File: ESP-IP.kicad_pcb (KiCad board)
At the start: 2 copper layers, 32 parts, among them J1 Serial and power, J2 Programming Pads, Q1 L78M05ABDT-TR, SW1 SW_Push, SW2 SW_Push, U1 ESP32-WROOM-32U, U3 TXS0102DCU, U4 AMS1117-3.3

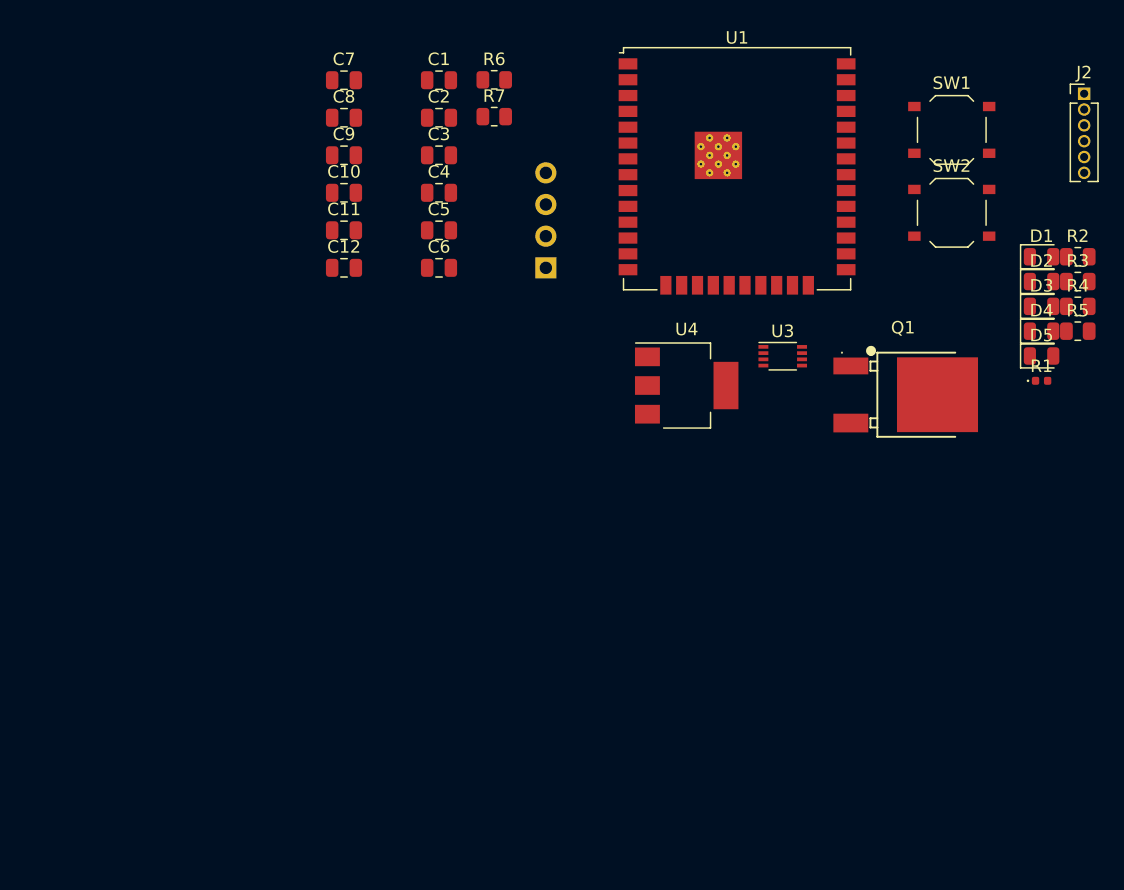
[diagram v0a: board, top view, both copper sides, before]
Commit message: my suggested board layout, includes schematic fixes, part number allocation and PCB, routing TBD
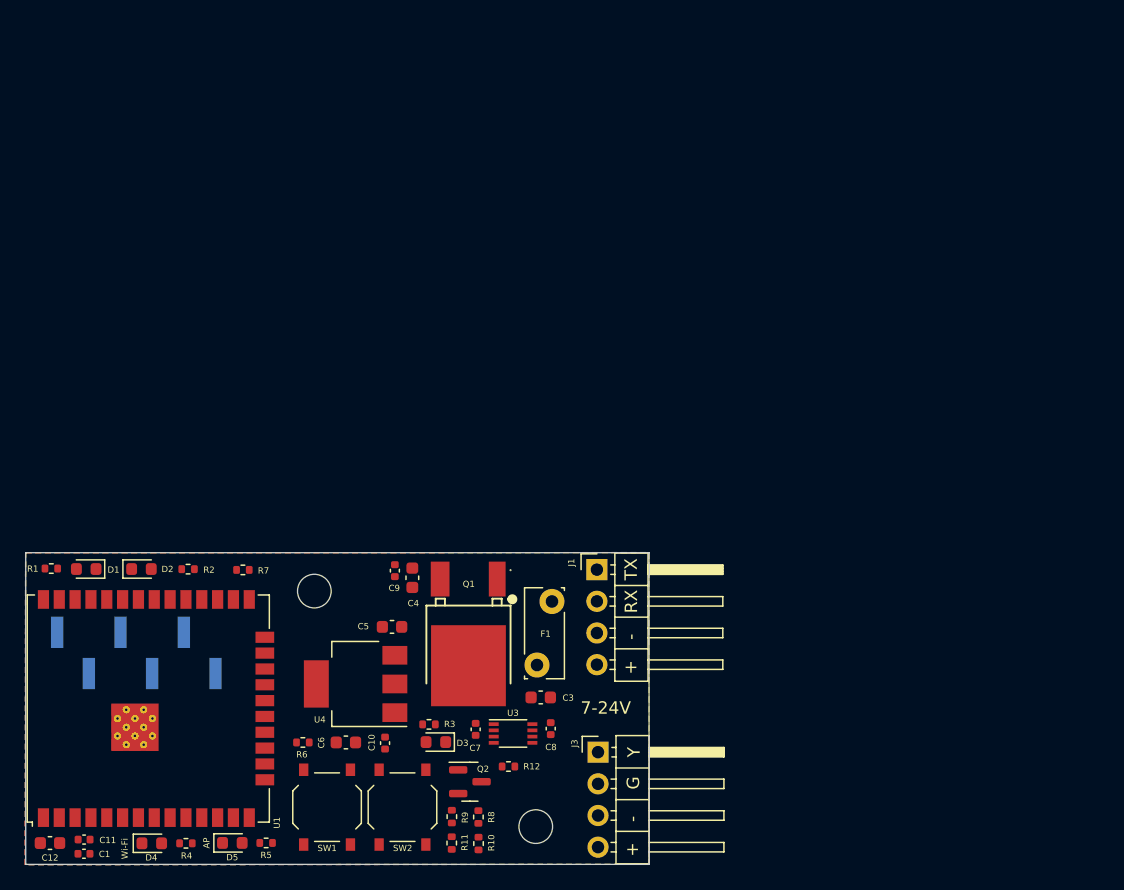
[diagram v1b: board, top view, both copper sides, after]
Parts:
- removed C2: 10uF, Capacitor_SMD:C_0805_2012Metric
- added F1: 250V 80mA, Fuse:Fuse_Bourns_MF-RG300, F.Cu at (116.1, 108.1)
- added H1: MountingHole, MountingHole:MountingHole_2.7mm_M2.5, F.Cu at (98.3, 102.1)
- added H2: MountingHole, MountingHole:MountingHole_2.7mm_M2.5, F.Cu at (116.0, 121.0)
- added J3: Comms and power, Connector_PinHeader_2.54mm:PinHeader_1x04_P2.54mm_Horizontal, F.Cu at (121.0, 115.0)
- added Q2: MMBT5551L, Package_TO_SOT_SMD:SOT-23, F.Cu at (110.7, 117.4)
- added R10: 10K, Resistor_SMD:R_0402_1005Metric, F.Cu at (111.4, 122.4)
- added R11: 10K, Resistor_SMD:R_0402_1005Metric, F.Cu at (109.3, 122.3)
- added R12: 1K, Resistor_SMD:R_0402_1005Metric, F.Cu at (113.8, 116.2)
- added R8: 33K, Resistor_SMD:R_0402_1005Metric, F.Cu at (111.4, 120.2)
- added R9: 33K, Resistor_SMD:R_0402_1005Metric, F.Cu at (109.3, 120.2)
- C1, C10, C11, C7, C8, C9: footprint Capacitor_SMD:C_0805_2012Metric -> Capacitor_SMD:C_0402_1005Metric
- C12, C3, C4, C5, C6: footprint Capacitor_SMD:C_0805_2012Metric -> Capacitor_SMD:C_0603_1608Metric
- D1, D2, D3, D4, D5: footprint LED_SMD:LED_0805_2012Metric -> LED_SMD:LED_0603_1608Metric
- J1: footprint Connector_PinSocket_2.54mm:PinSocket_1x04_P2.54mm_Vertical -> Connector_PinHeader_2.54mm:PinHeader_1x04_P2.54mm_Horizontal; moved to F.Cu
- J2: footprint Connector_PinHeader_1.27mm:PinHeader_1x06_P1.27mm_Vertical -> Connector_PinHeader_2.54mm:PinHeader_1x06_P2.54mm_Vertical_SMD_Pin1Left; moved to B.Cu
- R1: value 1k -> 1K; footprint LED_SMD:LED_0402_1005Metric -> Resistor_SMD:R_0402_1005Metric
- R2, R3, R4, R5: value 1k -> 1K; footprint Resistor_SMD:R_0805_2012Metric -> Resistor_SMD:R_0402_1005Metric
- R6, R7: value 10k -> 10K; footprint Resistor_SMD:R_0805_2012Metric -> Resistor_SMD:R_0402_1005Metric
- moved J2 88.3 mm to (84.0, 107.1), turned to -90 degrees
- moved R4 83.5 mm to (88.0, 122.4), turned to 180 degrees
- moved D4 82.4 mm to (85.2, 122.4)
- moved R1 80.9 mm to (77.2, 100.3)
- moved D1 80.6 mm to (80.0, 100.4), turned to 180 degrees
- moved R5 77.0 mm to (94.4, 122.3), turned to 180 degrees
- moved D2 75.8 mm to (84.4, 100.4)
- moved D5 75.8 mm to (91.7, 122.3)
- moved R2 75.6 mm to (88.1, 100.4), turned to 180 degrees
- moved SW1 73.9 mm to (99.3, 119.5), turned to 90 degrees
- moved C1 68.3 mm to (79.8, 123.2)
- moved SW2 64.9 mm to (105.3, 119.5), turned to 90 degrees
- moved U1 64.1 mm to (85.0, 111.5), turned to 90 degrees
- moved R3 63.0 mm to (107.5, 112.8), turned to 180 degrees
- moved D3 59.9 mm to (108.0, 114.2), turned to 180 degrees
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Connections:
- Q1 pad 1: +BATT -> Net-(Q1-IN)
- Q1 pad 3: 5V -> +5V
- U1 pad 14: unconnected-(U1-IO12-Pad14) -> AP_STATUS
- U1 pad 16: unconnected-(U1-IO13-Pad16) -> WIFI_STATUS
- U1 pad 30: unconnected-(U1-IO18-Pad30) -> dscClock
- U1 pad 31: unconnected-(U1-IO19-Pad31) -> dscRead
- U1 pad 33: unconnected-(U1-IO21-Pad33) -> dscWrite
- U1 pad 6: AP_STATUS -> unconnected-(U1-IO34-Pad6)
- U1 pad 7: WIFI_STATUS -> unconnected-(U1-IO35-Pad7)
- U3 pad 6: unconnected-(U3-OE-Pad6) -> +3V3
- U4 pad 3: 5V -> +5V
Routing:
- added copper zone on In2.Cu, net +3V3
- added copper zone on B.Cu, net GND
- added copper zone on F.Cu, net GND
- added copper zone on In1.Cu, net GND
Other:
- board outline added: 50 x 25 mm
- copper layers 2 -> 4
- board text added: "+"
- board text added: "-"
- board text added: "0"
- board text added: "0 mm"
- board text added: "0,01 mm"
- board text added: "0,0152 mm"
- board text added: "0,02"
- board text added: "0,035 mm"
- board text added: "0,2104 mm"
- board text added: "1"
- board text added: "1,065 mm"
- board text added: "3,3"
- board text added: "3V3"
- board text added: "4,5"
- board text added: "7-24V"
- board text added: "7628"
- board text added: "AP"
- board text added: "B.Cu"
- board text added: "B.Mask"
- board text added: "B.Paste"
- board text added: "B.Silkscreen"
- board text added: "Bottom Silk Screen"
- board text added: "Bottom Solder Mask"
- board text added: "Bottom Solder Paste"
- board text added: "Color"
- board text added: "Dielectric 1"
- board text added: "Dielectric 2"
- board text added: "Dielectric 3"
- board text added: "EN"
- board text added: "Epsilon R"
- board text added: "F.Cu"
- board text added: "F.Mask"
- board text added: "F.Paste"
- board text added: "F.Silkscreen"
- board text added: "FR4"
- board text added: "G"
- board text added: "GND"
- board text added: "IO0"
- board text added: "In1.Cu"
- board text added: "In2.Cu"
- board text added: "Layer Name"
- board text added: "Loss Tangent"
- board text added: "Material"
- board text added: "Not specified"
- board text added: "RX"
- board text added: "RXD"
- board text added: "TX"
- board text added: "TXD"
- board text added: "Thickness (mm)"
- board text added: "Top Silk Screen"
- board text added: "Top Solder Mask"
- board text added: "Top Solder Paste"
- board text added: "Type"
- board text added: "Wi-Fi"
- board text added: "Y"
- board text added: "copper"
- board text added: "core"
- board text added: "prepreg"
